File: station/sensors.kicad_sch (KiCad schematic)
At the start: 14 parts, among them J4 BME280, J5 WIND_SENSOR, J6 RAIN_SENSOR, J7 SOIL_MOISTURE, J8 SOIL_MOISTURE, U3 LIGHT_SENSOR

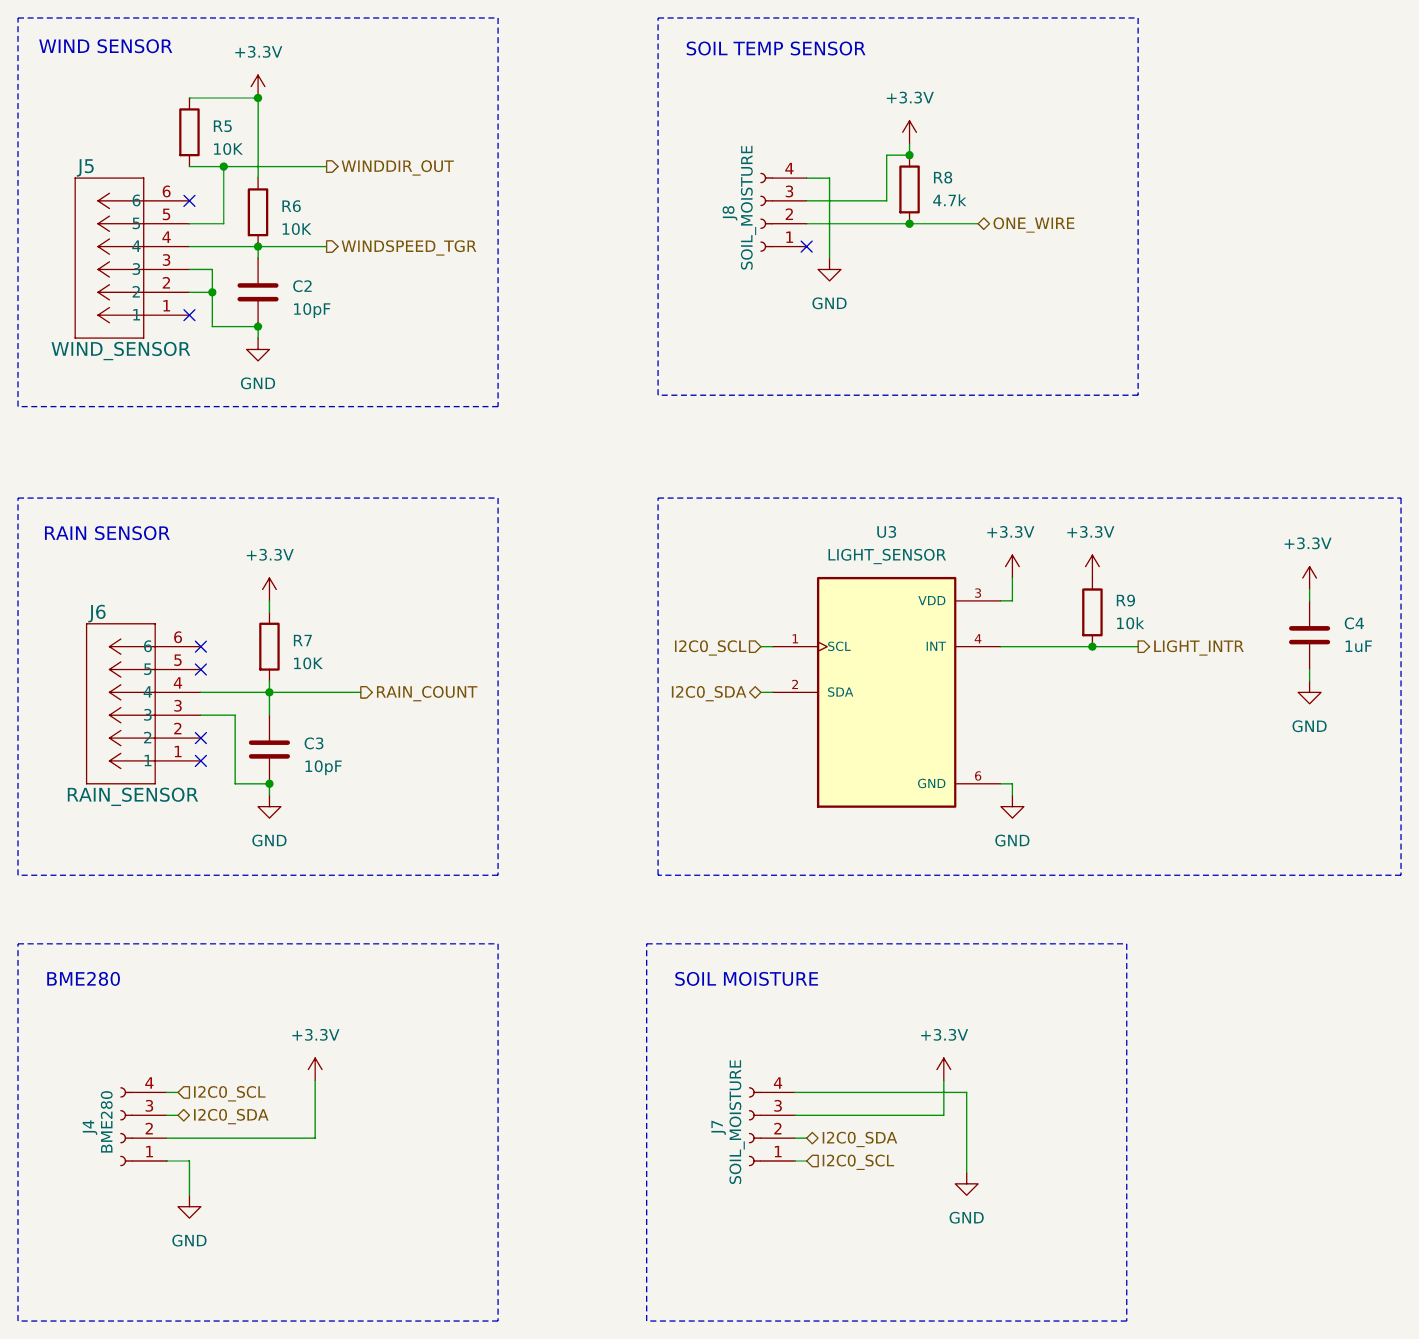
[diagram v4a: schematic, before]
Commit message: Added a reset button, status LEDs and broke out UART pins
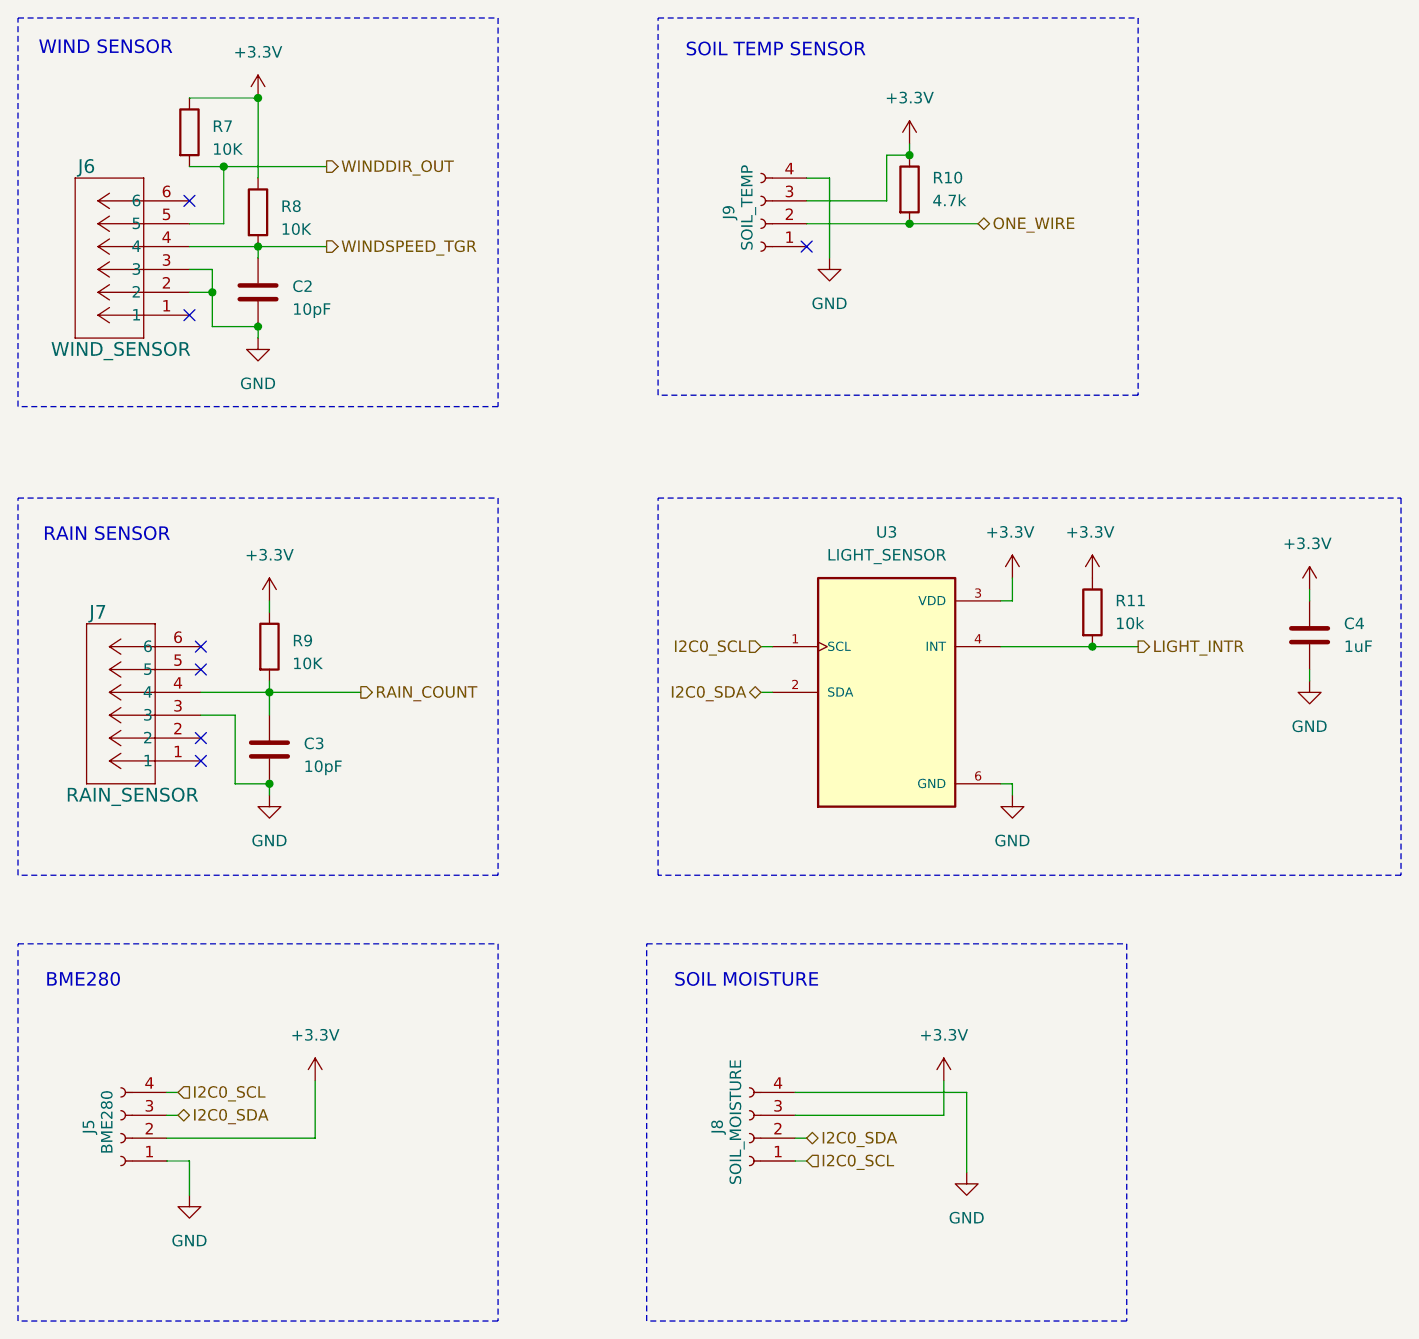
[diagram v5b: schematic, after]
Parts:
- J9: renamed from J8; value SOIL_MOISTURE -> SOIL_TEMP
- R10: renamed from R8; footprint (none) -> Resistor_SMD:R_0805_2012Metric_Pad1.20x1.40mm_HandSolder
- renumbered J4 to J5, J5 to J6, J6 to J7, J7 to J8, R9 to R11, R5 to R7, R6 to R8, R7 to R9
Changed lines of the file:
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@@
 		(dnp no)
 		(fields_autoplaced yes)
-		(property "Reference" "R8"
+		(property "Reference" "R10"
 			(at 127 41.9099 0)
 			(effects
@@
 			)
 		)
-		(property "Footprint" ""
+		(property "Footprint" "Resistor_SMD:R_0805_2012Metric_Pad1.20x1.40mm_HandSolder"
 			(at 122.682 43.18 90)
 			(effects
@@
 			(project "weather_station_pico"
 				(path "/8f1f45aa-e764-4c95-a223-c466cf9a95bf/7a04e3d1-638a-4686-bfce-e4e7db2cefc8"
-					(reference "R8")
+					(reference "R10")
 					(unit 1)
 				)
@@
 		(dnp no)
 		(fields_autoplaced yes)
-		(property "Reference" "#PWR025"
+		(property "Reference" "#PWR031"
 			(at 130.81 158.75 0)
 			(effects
@@
 			(project "weather_station_pico"
 				(path "/8f1f45aa-e764-4c95-a223-c466cf9a95bf/7a04e3d1-638a-4686-bfce-e4e7db2cefc8"
-					(reference "#PWR025")
+					(reference "#PWR031")
 					(unit 1)
 				)
@@
 		(on_board yes)
 		(dnp no)
-		(property "Reference" "#PWR031"
+		(property "Reference" "#PWR035"
 			(at 168.91 91.44 0)
 			(effects
@@
 			(project "weather_station_pico"
 				(path "/8f1f45aa-e764-4c95-a223-c466cf9a95bf/7a04e3d1-638a-4686-bfce-e4e7db2cefc8"
-					(reference "#PWR031")
+					(reference "#PWR035")
 					(unit 1)
 				)
@@
 		(dnp no)
 		(fields_autoplaced yes)
-		(property "Reference" "R7"
+		(property "Reference" "R9"
 			(at 55.88 93.345 0)
 			(effects
@@
 			(project "weather_station_pico"
 				(path "/8f1f45aa-e764-4c95-a223-c466cf9a95bf/7a04e3d1-638a-4686-bfce-e4e7db2cefc8"
-					(reference "R7")
+					(reference "R9")
 					(unit 1)
 				)
@@
 		(dnp no)
 		(fields_autoplaced yes)
-		(property "Reference" "#PWR021"
+		(property "Reference" "#PWR025"
 			(at 53.34 92.71 0)
 			(effects
@@
 			(project "weather_station_pico"
 				(path "/8f1f45aa-e764-4c95-a223-c466cf9a95bf/7a04e3d1-638a-4686-bfce-e4e7db2cefc8"
-					(reference "#PWR021")
+					(reference "#PWR025")
 					(unit 1)
 				)
@@
 		(dnp no)
 		(fields_autoplaced yes)
-		(property "Reference" "#PWR026"
+		(property "Reference" "#PWR028"
 			(at 115.57 57.15 0)
 			(effects
@@
 			(project "weather_station_pico"
 				(path "/8f1f45aa-e764-4c95-a223-c466cf9a95bf/7a04e3d1-638a-4686-bfce-e4e7db2cefc8"
-					(reference "#PWR026")
+					(reference "#PWR028")
 					(unit 1)
 				)
@@
 		(dnp no)
 		(fields_autoplaced yes)
-		(property "Reference" "#PWR029"
+		(property "Reference" "#PWR033"
 			(at 135.89 116.84 0)
 			(effects
@@
 			(project "weather_station_pico"
 				(path "/8f1f45aa-e764-4c95-a223-c466cf9a95bf/7a04e3d1-638a-4686-bfce-e4e7db2cefc8"
-					(reference "#PWR029")
+					(reference "#PWR033")
 					(unit 1)
 				)
@@
 		(dnp no)
 		(fields_autoplaced yes)
-		(property "Reference" "#PWR022"
+		(property "Reference" "#PWR026"
 			(at 53.34 116.84 0)
 			(effects
@@
 			(project "weather_station_pico"
 				(path "/8f1f45aa-e764-4c95-a223-c466cf9a95bf/7a04e3d1-638a-4686-bfce-e4e7db2cefc8"
-					(reference "#PWR022")
+					(reference "#PWR026")
 					(unit 1)
 				)
@@
 		(dnp no)
 		(fields_autoplaced yes)
-		(property "Reference" "#PWR019"
+		(property "Reference" "#PWR023"
 			(at 52.07 36.83 0)
 			(effects
@@
 			(project "weather_station_pico"
 				(path "/8f1f45aa-e764-4c95-a223-c466cf9a95bf/7a04e3d1-638a-4686-bfce-e4e7db2cefc8"
-					(reference "#PWR019")
+					(reference "#PWR023")
 					(unit 1)
 				)
@@
 		(on_board yes)
 		(dnp no)
-		(property "Reference" "J5"
+		(property "Reference" "J6"
 			(at 33.02 40.64 0)
 			(effects
@@
 			(project "weather_station_pico"
 				(path "/8f1f45aa-e764-4c95-a223-c466cf9a95bf/7a04e3d1-638a-4686-bfce-e4e7db2cefc8"
-					(reference "J5")
+					(reference "J6")
 					(unit 1)
 				)
@@
 		(dnp no)
 		(fields_autoplaced yes)
-		(property "Reference" "#PWR020"
+		(property "Reference" "#PWR024"
 			(at 52.07 66.04 0)
 			(effects
@@
 			(project "weather_station_pico"
 				(path "/8f1f45aa-e764-4c95-a223-c466cf9a95bf/7a04e3d1-638a-4686-bfce-e4e7db2cefc8"
-					(reference "#PWR020")
+					(reference "#PWR024")
 					(unit 1)
 				)
@@
 		(dnp no)
 		(fields_autoplaced yes)
-		(property "Reference" "R6"
+		(property "Reference" "R8"
 			(at 54.61 45.085 0)
 			(effects
@@
 			(project "weather_station_pico"
 				(path "/8f1f45aa-e764-4c95-a223-c466cf9a95bf/7a04e3d1-638a-4686-bfce-e4e7db2cefc8"
-					(reference "R6")
+					(reference "R8")
 					(unit 1)
 				)
@@
 		(on_board yes)
 		(dnp no)
-		(property "Reference" "J7"
+		(property "Reference" "J8"
 			(at 103.124 147.32 90)
 			(effects
@@
 			(project "weather_station_pico"
 				(path "/8f1f45aa-e764-4c95-a223-c466cf9a95bf/7a04e3d1-638a-4686-bfce-e4e7db2cefc8"
-					(reference "J7")
+					(reference "J8")
 					(unit 1)
 				)
@@
 		(dnp no)
 		(fields_autoplaced yes)
-		(property "Reference" "#PWR023"
+		(property "Reference" "#PWR027"
 			(at 58.42 146.05 0)
 			(effects
@@
 			(project "weather_station_pico"
 				(path "/8f1f45aa-e764-4c95-a223-c466cf9a95bf/7a04e3d1-638a-4686-bfce-e4e7db2cefc8"
-					(reference "#PWR023")
+					(reference "#PWR027")
 					(unit 1)
 				)
@@
 		(on_board yes)
 		(dnp no)
-		(property "Reference" "J4"
+		(property "Reference" "J5"
 			(at 33.274 147.32 90)
 			(effects
@@
 			(project "weather_station_pico"
 				(path "/8f1f45aa-e764-4c95-a223-c466cf9a95bf/7a04e3d1-638a-4686-bfce-e4e7db2cefc8"
-					(reference "J4")
+					(reference "J5")
 					(unit 1)
 				)
@@
 		(dnp no)
 		(fields_autoplaced yes)
-		(property "Reference" "R5"
+		(property "Reference" "R7"
 			(at 46.99 36.195 0)
 			(effects
@@
 			(project "weather_station_pico"
 				(path "/8f1f45aa-e764-4c95-a223-c466cf9a95bf/7a04e3d1-638a-4686-bfce-e4e7db2cefc8"
-					(reference "R5")
+					(reference "R7")
 					(unit 1)
 				)
@@
 		(dnp no)
 		(fields_autoplaced yes)
-		(property "Reference" "R9"
+		(property "Reference" "R11"
 			(at 147.32 88.8999 0)
 			(effects
@@
 			(project "weather_station_pico"
 				(path "/8f1f45aa-e764-4c95-a223-c466cf9a95bf/7a04e3d1-638a-4686-bfce-e4e7db2cefc8"
-					(reference "R9")
+					(reference "R11")
 					(unit 1)
 				)
@@
 		(dnp no)
 		(fields_autoplaced yes)
-		(property "Reference" "#PWR018"
+		(property "Reference" "#PWR022"
 			(at 44.45 161.29 0)
 			(effects
@@
 			(project "weather_station_pico"
 				(path "/8f1f45aa-e764-4c95-a223-c466cf9a95bf/7a04e3d1-638a-4686-bfce-e4e7db2cefc8"
-					(reference "#PWR018")
+					(reference "#PWR022")
 					(unit 1)
 				)
@@
 		(on_board yes)
 		(dnp no)
-		(property "Reference" "#PWR028"
+		(property "Reference" "#PWR032"
 			(at 135.89 90.17 0)
 			(effects
@@
 			(project "weather_station_pico"
 				(path "/8f1f45aa-e764-4c95-a223-c466cf9a95bf/7a04e3d1-638a-4686-bfce-e4e7db2cefc8"
-					(reference "#PWR028")
+					(reference "#PWR032")
 					(unit 1)
 				)
@@
 		(on_board yes)
 		(dnp no)
-		(property "Reference" "J8"
+		(property "Reference" "J9"
 			(at 104.394 45.72 90)
 			(effects
@@
 			)
 		)
-		(property "Value" "SOIL_MOISTURE"
+		(property "Value" "SOIL_TEMP"
 			(at 106.426 45.212 90)
 			(effects
@@
 			(project "weather_station_pico"
 				(path "/8f1f45aa-e764-4c95-a223-c466cf9a95bf/7a04e3d1-638a-4686-bfce-e4e7db2cefc8"
-					(reference "J8")
+					(reference "J9")
 					(unit 1)
 				)
@@
 		(on_board yes)
 		(dnp no)
-		(property "Reference" "#PWR030"
+		(property "Reference" "#PWR034"
 			(at 144.78 90.17 0)
 			(effects
@@
 			(project "weather_station_pico"
 				(path "/8f1f45aa-e764-4c95-a223-c466cf9a95bf/7a04e3d1-638a-4686-bfce-e4e7db2cefc8"
-					(reference "#PWR030")
+					(reference "#PWR034")
 					(unit 1)
 				)
@@
 		(on_board yes)
 		(dnp no)
-		(property "Reference" "J6"
+		(property "Reference" "J7"
 			(at 34.29 90.17 0)
 			(effects
@@
 			(project "weather_station_pico"
 				(path "/8f1f45aa-e764-4c95-a223-c466cf9a95bf/7a04e3d1-638a-4686-bfce-e4e7db2cefc8"
-					(reference "J6")
+					(reference "J7")
 					(unit 1)
 				)
@@
 		(dnp no)
 		(fields_autoplaced yes)
-		(property "Reference" "#PWR027"
+		(property "Reference" "#PWR030"
 			(at 128.27 146.05 0)
 			(effects
@@
 			(project "weather_station_pico"
 				(path "/8f1f45aa-e764-4c95-a223-c466cf9a95bf/7a04e3d1-638a-4686-bfce-e4e7db2cefc8"
-					(reference "#PWR027")
+					(reference "#PWR030")
 					(unit 1)
 				)
@@
 		(dnp no)
 		(fields_autoplaced yes)
-		(property "Reference" "#PWR032"
+		(property "Reference" "#PWR036"
 			(at 168.91 104.14 0)
 			(effects
@@
 			(project "weather_station_pico"
 				(path "/8f1f45aa-e764-4c95-a223-c466cf9a95bf/7a04e3d1-638a-4686-bfce-e4e7db2cefc8"
-					(reference "#PWR032")
+					(reference "#PWR036")
 					(unit 1)
 				)
@@
 		(dnp no)
 		(fields_autoplaced yes)
-		(property "Reference" "#PWR024"
+		(property "Reference" "#PWR029"
 			(at 124.46 41.91 0)
 			(effects
@@
 			(project "weather_station_pico"
 				(path "/8f1f45aa-e764-4c95-a223-c466cf9a95bf/7a04e3d1-638a-4686-bfce-e4e7db2cefc8"
-					(reference "#PWR024")
-					(unit 1)
-				)
+					(reference "#PWR029")
+					(unit 1)
+				)
